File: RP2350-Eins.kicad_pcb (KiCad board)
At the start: 4 copper layers, 68.6 x 53.3 mm, 72 parts, among them J1 CONN_PWR, J10 CONN_USB, J2 CONN_ICSP, J3 CONN_A, J4 CONN_P, J5 CONN_X, J6 CONN_DBG, J7 CONN_JTAG, J8 CONN_D1, J9 CONN_D2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

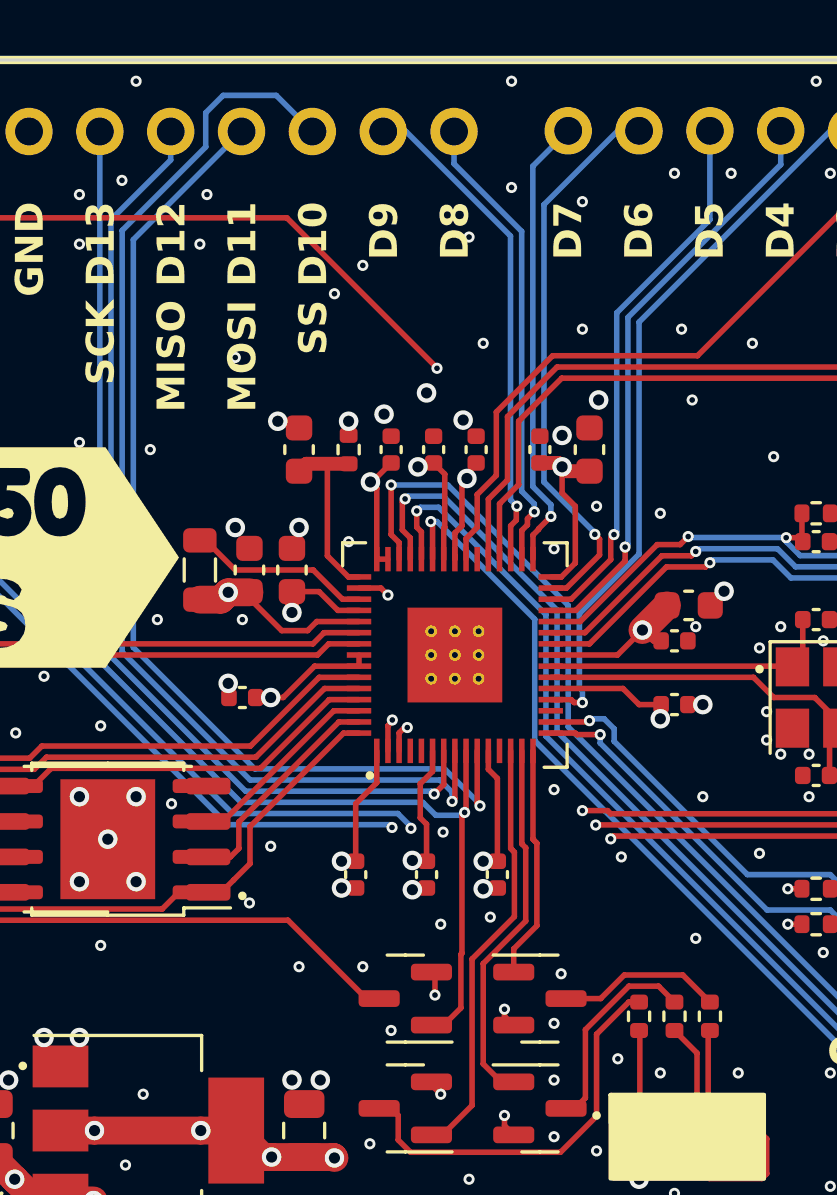
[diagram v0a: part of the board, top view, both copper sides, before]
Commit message: Moved staff around.
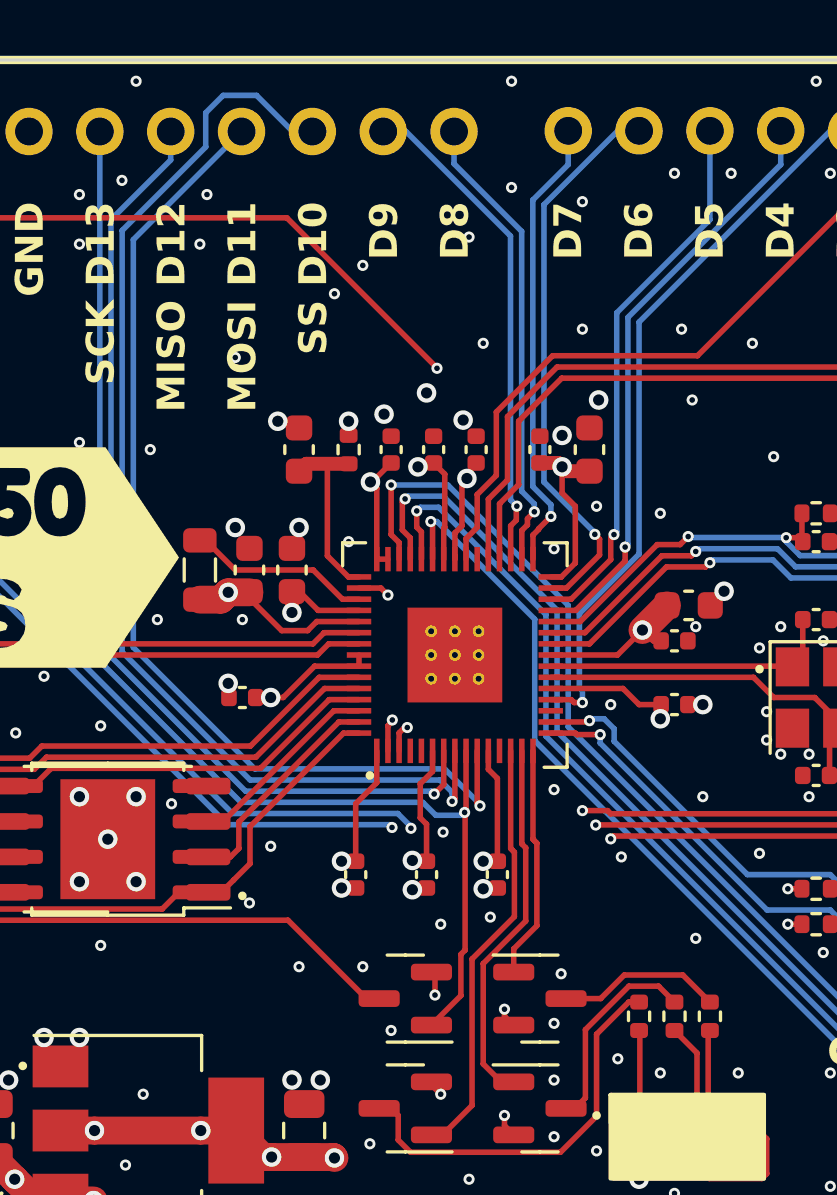
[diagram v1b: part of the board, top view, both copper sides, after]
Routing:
- net GND: vias 221 -> 222
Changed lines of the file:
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@@
 	)
 	(segment
-		(start 165.2185 93.396)
-		(end 164.458314 93.396)
-		(width 0.2)
-		(layer "F.Cu")
-		(net 1)
-	)
-	(segment
 		(start 162.052 96.52)
 		(end 161.516 96.52)
@@
 	)
 	(segment
+		(start 163.754 93.396)
+		(end 163.081 92.723)
+		(width 0.2)
+		(layer "F.Cu")
+		(net 1)
+	)
+	(segment
 		(start 164.846 87.12)
 		(end 164.846 86.614)
@@
 	)
 	(segment
-		(start 163.785314 92.723)
-		(end 162.814 92.723)
-		(width 0.2)
-		(layer "F.Cu")
-		(net 1)
-	)
-	(segment
 		(start 182.12 89.916)
 		(end 182.626 89.916)
@@
 	)
 	(segment
+		(start 165.2185 93.396)
+		(end 163.754 93.396)
+		(width 0.2)
+		(layer "F.Cu")
+		(net 1)
+	)
+	(segment
 		(start 181.1 104.648)
 		(end 180.594 104.648)
@@
 	)
 	(segment
+		(start 163.081 92.723)
+		(end 162.814 92.723)
+		(width 0.2)
+		(layer "F.Cu")
+		(net 1)
+	)
+	(segment
 		(start 162.502314 96.52)
 		(end 163.626314 95.396)
@@
 	)
 	(segment
-		(start 164.458314 93.396)
-		(end 163.785314 92.723)
-		(width 0.2)
-		(layer "F.Cu")
-		(net 1)
-	)
-	(segment
 		(start 159.545 112.047)
 		(end 160.815 112.047)
@@
 	)
 	(via
+		(at 174.244 96.774)
+		(size 0.4)
+		(drill 0.2)
+		(layers "F.Cu" "B.Cu")
+		(free yes)
+		(net 4)
+	)
+	(via
 		(at 187.198 83.82)
 		(size 0.4)
@@
 	)
 	(segment
-		(start 171.45 77.47)
-		(end 172.72 76.2)
+		(start 172.098723 90.029277)
+		(end 172.098723 89.606409)
 		(width 0.2)
 		(layer "B.Cu")
@@
 	)
 	(segment
-		(start 172.098723 90.029277)
-		(end 172.098723 89.606409)
+		(start 172.72 77.412314)
+		(end 172.72 76.2)
 		(width 0.2)
 		(layer "B.Cu")
@@
 	(segment
 		(start 171.45 88.957686)
-		(end 171.45 77.47)
+		(end 171.45 78.682314)
+		(width 0.2)
+		(layer "B.Cu")
+		(net 19)
+	)
+	(segment
+		(start 171.45 78.682314)
+		(end 172.72 77.412314)
 		(width 0.2)
 		(layer "B.Cu")
@@
 	)
 	(segment
-		(start 162.251 74.93)
-		(end 163.546 76.225)
+		(start 159.722496 75.554831)
+		(end 160.347327 74.93)
 		(width 0.2)
 		(layer "B.Cu")
@@
 	)
 	(segment
-		(start 156.726 94.888628)
-		(end 156.726 79.773811)
+		(start 156.726 79.773811)
+		(end 159.722496 76.777315)
 		(width 0.2)
 		(layer "B.Cu")
@@
 	)
 	(segment
-		(start 159.722496 75.554831)
-		(end 160.347327 74.93)
+		(start 161.544 74.93)
+		(end 162.839 76.225)
 		(width 0.2)
 		(layer "B.Cu")
@@
 	)
 	(segment
-		(start 156.726 79.773811)
-		(end 159.722496 76.777315)
+		(start 168.556 100.242659)
+		(end 168.556 99.913896)
 		(width 0.2)
 		(layer "B.Cu")
@@
 	)
 	(segment
-		(start 159.722496 76.777315)
-		(end 159.722496 75.554831)
+		(start 168.556 99.913896)
+		(end 168.121341 99.479237)
 		(width 0.2)
 		(layer "B.Cu")
@@
 	)
 	(segment
-		(start 168.556 100.242659)
-		(end 168.556 99.913896)
+		(start 168.121341 99.479237)
+		(end 161.316609 99.479237)
 		(width 0.2)
 		(layer "B.Cu")
@@
 	)
 	(segment
-		(start 168.556 99.913896)
-		(end 168.121341 99.479237)
+		(start 159.722496 76.777315)
+		(end 159.722496 75.554831)
 		(width 0.2)
 		(layer "B.Cu")
@@
 	)
 	(segment
-		(start 168.121341 99.479237)
-		(end 161.316609 99.479237)
+		(start 162.839 76.225)
+		(end 163.546 76.225)
+		(width 0.2)
+		(layer "B.Cu")
+		(net 22)
+	)
+	(segment
+		(start 156.726 94.888628)
+		(end 156.726 79.773811)
 		(width 0.2)
 		(layer "B.Cu")
@@
 	(segment
 		(start 160.347327 74.93)
-		(end 162.251 74.93)
+		(end 161.544 74.93)
 		(width 0.2)
 		(layer "B.Cu")
@@
 	)
 	(segment
-		(start 168.91 105.691286)
-		(end 168.872 105.729286)
-		(width 0.2)
-		(layer "F.Cu")
-		(net 25)
-	)
-	(segment
-		(start 168.91 100.735717)
-		(end 168.91 105.691286)
+		(start 168.872 105.729286)
+		(end 168.872 107.2085)
 		(width 0.2)
 		(layer "F.Cu")
@@
 	)
 	(segment
-		(start 168.257768 108.265)
-		(end 167.8155 108.265)
+		(start 169.004501 100.641216)
+		(end 169.022 100.658715)
 		(width 0.2)
 		(layer "F.Cu")
@@
 	)
 	(segment
-		(start 168.872 105.729286)
-		(end 168.872 107.650768)
+		(start 169.022 105.579286)
+		(end 168.872 105.729286)
 		(width 0.2)
 		(layer "F.Cu")
@@
 	)
 	(segment
-		(start 169.056 100.589717)
-		(end 169.056 98.4335)
+		(start 169.022 100.658715)
+		(end 169.022 105.579286)
 		(width 0.2)
 		(layer "F.Cu")
@@
 	)
 	(segment
-		(start 169.004501 100.641216)
-		(end 168.91 100.735717)
+		(start 169.056 100.589717)
+		(end 169.056 98.4335)
 		(width 0.2)
 		(layer "F.Cu")
@@
 	)
 	(segment
-		(start 168.872 107.650768)
-		(end 168.257768 108.265)
+		(start 168.872 107.2085)
+		(end 167.8155 108.265)
 		(width 0.2)
 		(layer "F.Cu")

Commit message: Use manual vias under RP2350 instead of from footprint
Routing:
- net GND: vias 222 -> 227
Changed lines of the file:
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@@
 			(thermal_bridge_angle 45)
 		)
-		(pad "61" thru_hole circle
-			(at -0.85 -0.85 90)
-			(size 0.425 0.425)
-			(drill 0.2125)
-			(property pad_prop_heatsink)
-			(layers "*.Cu" "*.Mask")
-			(remove_unused_layers no)
-			(net 4 "GND")
-			(pinfunction "GND")
-			(pintype "passive")
-		)
-		(pad "61" thru_hole circle
-			(at -0.85 0 90)
-			(size 0.425 0.425)
-			(drill 0.2125)
-			(property pad_prop_heatsink)
-			(layers "*.Cu" "*.Mask")
-			(remove_unused_layers no)
-			(net 4 "GND")
-			(pinfunction "GND")
-			(pintype "passive")
-		)
-		(pad "61" thru_hole circle
-			(at -0.85 0.85 90)
-			(size 0.425 0.425)
-			(drill 0.2125)
-			(property pad_prop_heatsink)
-			(layers "*.Cu" "*.Mask")
-			(remove_unused_layers no)
-			(net 4 "GND")
-			(pinfunction "GND")
-			(pintype "passive")
-		)
-		(pad "61" thru_hole circle
-			(at 0 -0.85 90)
-			(size 0.425 0.425)
-			(drill 0.2125)
-			(property pad_prop_heatsink)
-			(layers "*.Cu" "*.Mask")
-			(remove_unused_layers no)
-			(net 4 "GND")
-			(pinfunction "GND")
-			(pintype "passive")
-		)
-		(pad "61" thru_hole circle
-			(at 0 0 90)
-			(size 0.425 0.425)
-			(drill 0.2125)
-			(property pad_prop_heatsink)
-			(layers "*.Cu" "*.Mask")
-			(remove_unused_layers no)
-			(net 4 "GND")
-			(pinfunction "GND")
-			(pintype "passive")
-		)
 		(pad "61" smd rect
 			(at 0 0 90)
@@
 			(thermal_bridge_angle 45)
 		)
-		(pad "61" thru_hole circle
-			(at 0 0.85 90)
-			(size 0.425 0.425)
-			(drill 0.2125)
-			(property pad_prop_heatsink)
-			(layers "*.Cu" "*.Mask")
-			(remove_unused_layers no)
-			(net 4 "GND")
-			(pinfunction "GND")
-			(pintype "passive")
-		)
-		(pad "61" thru_hole circle
-			(at 0.85 -0.85 90)
-			(size 0.425 0.425)
-			(drill 0.2125)
-			(property pad_prop_heatsink)
-			(layers "*.Cu" "*.Mask")
-			(remove_unused_layers no)
-			(net 4 "GND")
-			(pinfunction "GND")
-			(pintype "passive")
-		)
-		(pad "61" thru_hole circle
-			(at 0.85 0 90)
-			(size 0.425 0.425)
-			(drill 0.2125)
-			(property pad_prop_heatsink)
-			(layers "*.Cu" "*.Mask")
-			(remove_unused_layers no)
-			(net 4 "GND")
-			(pinfunction "GND")
-			(pintype "passive")
-		)
-		(pad "61" thru_hole circle
-			(at 0.85 0.85 90)
-			(size 0.425 0.425)
-			(drill 0.2125)
-			(property pad_prop_heatsink)
-			(layers "*.Cu" "*.Mask")
-			(remove_unused_layers no)
-			(net 4 "GND")
-			(pinfunction "GND")
-			(pintype "passive")
-		)
-		(model "${KIPRJMOD}/lib/RP2350A-QFN60.step"
+		(model "C:/Users/AG/Documents/KiCad/7.0/projects/RP2350-ProMini/lib/RP2350A-QFN60.wrl"
 			(offset
 				(xyz 0 0 0)
@@
 	)
 	(via
+		(at 168.656 94.996)
+		(size 0.7)
+		(drill 0.4)
+		(layers "F.Cu" "B.Cu")
+		(net 4)
+	)
+	(via
 		(at 189.23 95.504)
 		(size 0.4)
@@
 	)
 	(via
+		(at 169.672 93.98)
+		(size 0.7)
+		(drill 0.4)
+		(layers "F.Cu" "B.Cu")
+		(net 4)
+	)
+	(via
 		(at 137.922 90.932)
 		(size 0.4)
@@
 	)
 	(via
+		(at 167.64 93.98)
+		(size 0.7)
+		(drill 0.4)
+		(layers "F.Cu" "B.Cu")
+		(net 4)
+	)
+	(via
 		(at 155.194 78.486)
 		(size 0.4)
@@
 	)
 	(via
+		(at 167.64 96.012)
+		(size 0.7)
+		(drill 0.4)
+		(layers "F.Cu" "B.Cu")
+		(net 4)
+	)
+	(via
 		(at 186.69 123.444)
 		(size 0.4)
@@
 		(net 4)
 	)
+	(via
+		(at 169.672 96.012)
+		(size 0.7)
+		(drill 0.4)
+		(layers "F.Cu" "B.Cu")
+		(net 4)
+	)
